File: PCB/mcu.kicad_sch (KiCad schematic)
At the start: 34 parts, among them J5 Conn_01x02, SW1 Boot, SW2 Reset, U4 ESP32-C3FH4X, Y1 40MHz

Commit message: Added battery charging circuit and created WiFi api in firmware + created simple server for esp to send data to
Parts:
- removed H1: MountingHole, MountingHole:MountingHole_2.2mm_M2_DIN965_Pad, symbol Mechanical:MountingHole
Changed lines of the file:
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@@
-	)
-	(symbol
-		(lib_id "Mechanical:MountingHole")
-		(at 46.99 163.83 0)
-		(unit 1)
-		(exclude_from_sim yes)
-		(in_bom no)
-		(on_board yes)
-		(dnp no)
-		(fields_autoplaced yes)
-		(property "Reference" "H1"
-			(at 49.53 162.5599 0)
-			(effects
-				(font
-					(size 1.27 1.27)
-				)
-				(justify left)
-			)
-		)
-		(property "Value" "MountingHole"
-			(at 49.53 165.0999 0)
-			(effects
-				(font
-					(size 1.27 1.27)
-				)
-				(justify left)
-				(hide yes)
-			)
-		)
-		(property "Footprint" "MountingHole:MountingHole_2.2mm_M2_DIN965_Pad"
-			(at 46.99 163.83 0)
-			(effects
-				(font
-					(size 1.27 1.27)
-				)
-				(hide yes)
-			)
-		)
-		(property "Datasheet" "~"
-			(at 46.99 163.83 0)
-			(effects
-				(font
-					(size 1.27 1.27)
-				)
-				(hide yes)
-			)
-		)
-		(property "Description" "Mounting Hole without connection"
-			(at 46.99 163.83 0)
-			(effects
-				(font
-					(size 1.27 1.27)
-				)
-				(hide yes)
-			)
-		)
-		(instances
-			(project "Plant-health-meter"
-				(path "/357055bf-c309-4d6b-a2fa-f5ee5ba59771/f878f43f-0ef0-4ca5-9286-ff16b4b716af"
-					(reference "H1")
-					(unit 1)
-				)
-			)
-		)
 	)
 	(symbol

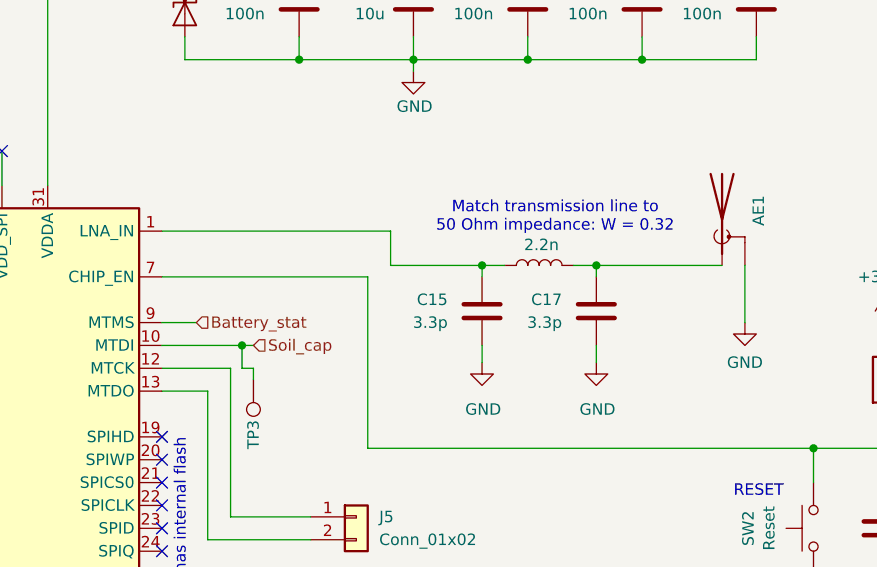
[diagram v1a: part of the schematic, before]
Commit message: Updated some component packages
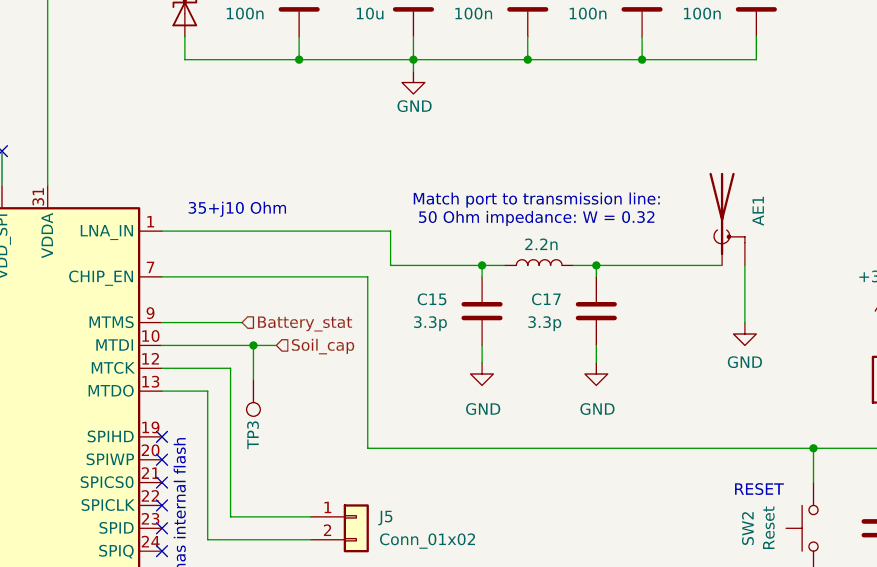
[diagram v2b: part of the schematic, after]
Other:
- note added: "35+j10 Ohm"
- note added: "Match port to transmission line: 50 Ohm impedance: W = 0.32"
- note removed: "Match transmission line to 50 Ohm impedance: W = 0.32"
